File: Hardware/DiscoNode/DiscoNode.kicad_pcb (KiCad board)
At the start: 2 copper layers, 76 x 76 mm, 71 parts, among them IC1 ATMEGA328P, J1 1267, J2 RJ45, J3 RJ45, J4 AVR-ISP-6, J5 Debug, J6 0026605020, Q1 NTR4003N, Q2 NTR4003N, Q3 NTR4003N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

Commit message: Fix LEDs
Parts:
- D1, D10, D11, D12, D13, D14, D15, D16, D17, D18, D2, D3, D4, D5, D6, D7, D8, D9: footprint LEDs:LED_RGB_PLCC-6 -> LEDs:LED_WS2812-PLCC6
- moved R8 1.78 mm to (124.0, 58.1)
- moved R7 1.72 mm to (126.0, 58.1)
- moved R17 1.63 mm to (151.1, 118.0)
- moved R16 1.60 mm to (149.1, 118.0)
- moved R9 1.05 mm to (129.8, 52.8)
- moved R13 1.03 mm to (170.6, 110.4)
- moved R14 1.03 mm to (172.4, 110.4)
- moved R15 1.03 mm to (174.3, 110.4)
- moved R10 1.00 mm to (170.3, 65.4)
- moved R11 1.00 mm to (172.2, 65.4)
- moved R12 1.00 mm to (174.1, 65.4)
- moved R18 0.96 mm to (145.2, 123.5), turned to 270 degrees
- moved D16 0.78 mm to (172.4, 119.5)
- moved R1 0.75 mm to (105.9, 114.5)
- moved R2 0.75 mm to (103.9, 114.5)
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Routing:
- net Net-(D8-Pad3): track 11.9 -> 0.00 mm
- net Net-(D8-Pad2): track 11.9 -> 0.00 mm
- net Net-(D8-Pad1): track 11.9 -> 0.00 mm
- net /LEDR: track 279.5 -> 283.3 mm
- net /LEDG: track 222.9 -> 219.5 mm
- net +12V: track 354.1 -> 350.8 mm
- net Net-(D11-Pad1): track 7.33 -> 4.04 mm
- net Net-(D7-Pad1): track 6.33 -> 3.39 mm
- net /LEDB: track 202.8 -> 200.3 mm
- net Net-(D11-Pad2): track 9.20 -> 7.06 mm
- net Net-(D16-Pad1): track 5.49 -> 3.46 mm
- net Net-(D5-Pad3): track 11.9 -> 10.0 mm
- net Net-(D5-Pad2): track 11.9 -> 10.0 mm
- net Net-(D5-Pad1): track 11.9 -> 10.0 mm
- net Net-(D4-Pad3): track 11.9 -> 10.0 mm
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
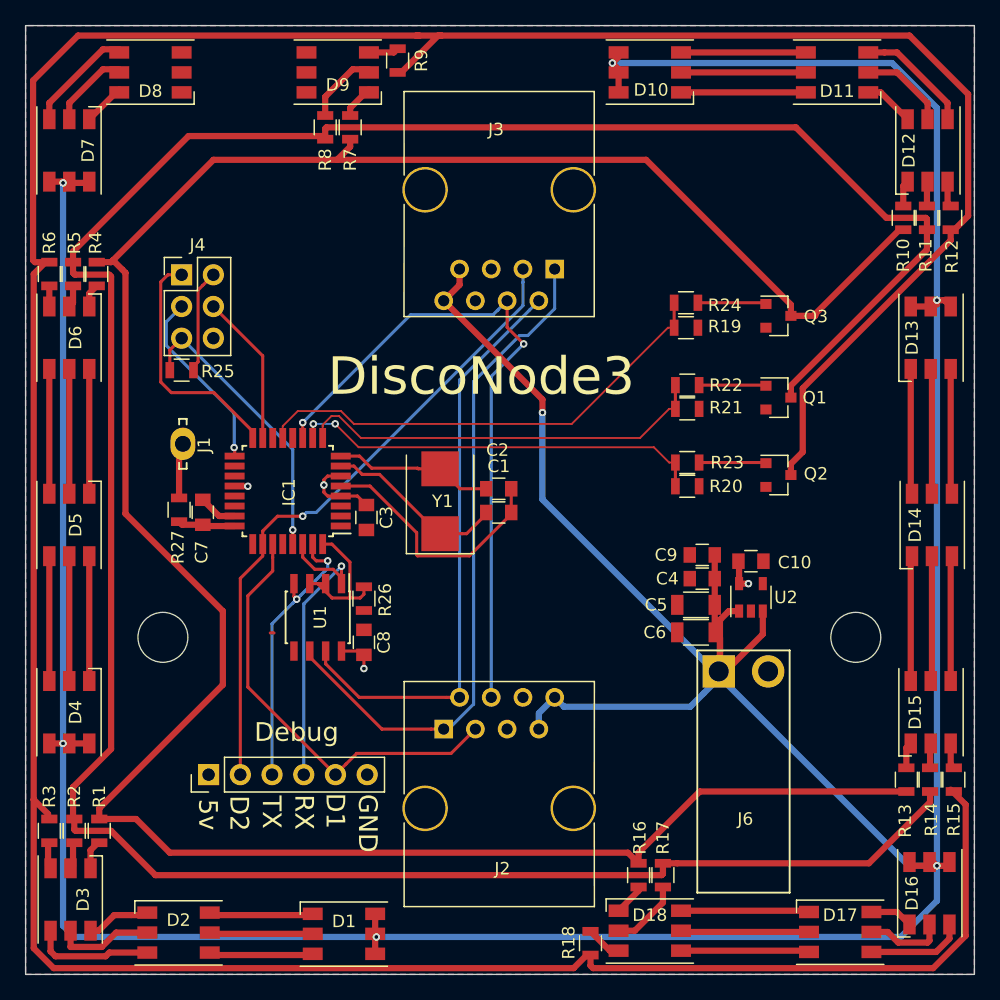
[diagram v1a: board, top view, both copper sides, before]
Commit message: Update LED & Crystal footprints. Change LED resistor placement.
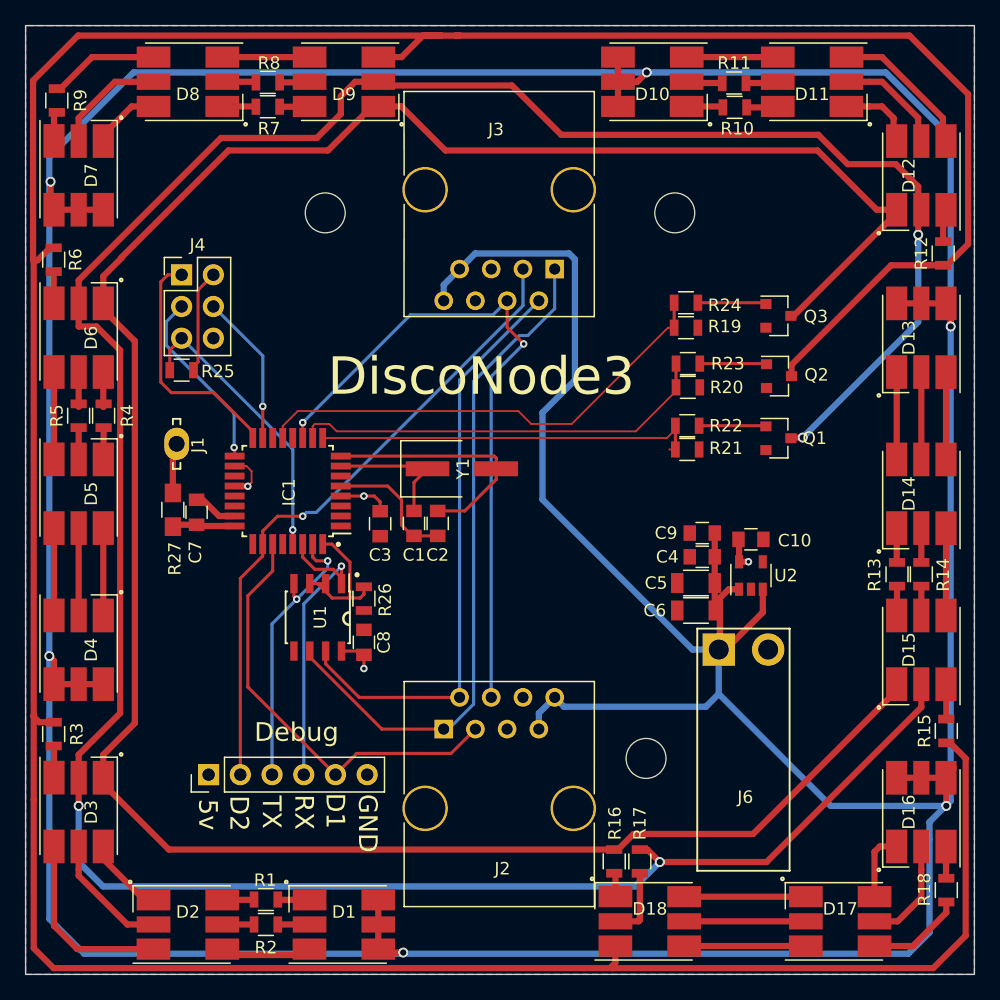
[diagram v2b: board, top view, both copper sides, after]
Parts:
- removed REF** (x2): MountingHole_4mm, Mounting_Holes:MountingHole_4mm
- added HOLE: MountingHole_3.2mm_M3, Mounting_Holes:MountingHole_3.2mm_M3, F.Cu at (152.0, 65.0)
- added HOLE: MountingHole_3.2mm_M3, Mounting_Holes:MountingHole_3.2mm_M3, F.Cu at (149.7, 108.7)
- added HOLE: MountingHole_3.2mm_M3, Mounting_Holes:MountingHole_3.2mm_M3, F.Cu at (124.0, 65.0)
- D1, D10, D11, D12, D13, D14, D15, D16, D17, D18, D2, D3, D4, D5, D6, D7, D8, D9: footprint LEDs:LED_WS2812-PLCC6 -> DiscoNode:LED_RGB-PLCC6-5.5x5.3mm
- IC1: value ATMEGA328P -> ATMEGA328PB-A
- R27: footprint Resistors_SMD:R_0805 -> Resistors_SMD:R_0805_HandSoldering
- Y1: footprint Crystals:Crystal_SMD_7050-2pin_7.0x5.0mm -> DiscoNode:Crystal_SMD_2pin_7.0x4.1mm
- moved R18 28.8 mm to (173.8, 119.2)
- moved R9 27.5 mm to (102.5, 56.0)
- moved R11 18.9 mm to (156.8, 54.6), turned to 0 degrees
- moved R2 17.1 mm to (119.2, 122.0), turned to 180 degrees
- moved R13 16.5 mm to (169.8, 94.0)
- moved R14 16.5 mm to (171.8, 94.0)
- moved R10 16.1 mm to (156.8, 56.5), turned to 0 degrees
- moved R1 14.4 mm to (119.2, 120.0), turned to 180 degrees
- moved R4 11.4 mm to (106.2, 81.2)
- moved R5 11.4 mm to (104.2, 81.2)
- moved R20 7.93 mm to (153.1, 79.0)
- moved Q2 7.93 mm to (160.3, 78.1)
- moved R23 7.93 mm to (153.1, 77.1)
- moved R3 7.76 mm to (102.2, 106.8)
- moved D3 7.03 mm to (104.2, 113.0)
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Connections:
- D11 pad 5: Net-(D10-Pad2) -> Net-(D11-Pad5)
- D11 pad 6: Net-(D10-Pad1) -> Net-(D11-Pad6)
- D12 pad 1: Net-(D12-Pad1) -> /LEDB
- D12 pad 2: Net-(D12-Pad2) -> /LEDG
- D15 pad 1: Net-(D15-Pad1) -> /LEDB
- D15 pad 2: Net-(D15-Pad2) -> /LEDG
- D15 pad 5: Net-(D14-Pad2) -> Net-(D15-Pad5)
- D15 pad 6: Net-(D14-Pad1) -> Net-(D15-Pad6)
- D17 pad 4: Net-(D16-Pad3) -> Net-(D17-Pad4)
- D18 pad 3: Net-(D18-Pad3) -> /LEDR
- D2 pad 5: Net-(D1-Pad2) -> Net-(D2-Pad5)
- D2 pad 6: Net-(D1-Pad1) -> Net-(D2-Pad6)
- D3 pad 1: Net-(D3-Pad1) -> /LEDB
- D3 pad 2: Net-(D3-Pad2) -> /LEDG
- D6 pad 1: Net-(D6-Pad1) -> /LEDB
- D6 pad 2: Net-(D6-Pad2) -> /LEDG
- D6 pad 5: Net-(D5-Pad2) -> Net-(D6-Pad5)
- D6 pad 6: Net-(D5-Pad1) -> Net-(D6-Pad6)
- D8 pad 4: Net-(D7-Pad3) -> Net-(D8-Pad4)
- D9 pad 1: Net-(D9-Pad1) -> /LEDB
- D9 pad 2: Net-(D9-Pad2) -> /LEDG
- D9 pad 3: Net-(D9-Pad3) -> /LEDR
- D9 pad 4: Net-(D8-Pad3) -> Net-(D9-Pad4)
- D9 pad 5: Net-(D8-Pad2) -> Net-(D9-Pad5)
- D9 pad 6: Net-(D8-Pad1) -> Net-(D9-Pad6)
- IC1 pad 3: GND -> Net-(IC1-Pad3)
- IC1 pad 6: +5V -> Net-(IC1-Pad6)
- R1 pad 1: Net-(D3-Pad1) -> Net-(D1-Pad1)
- R1 pad 2: /LEDB -> Net-(D2-Pad6)
- R10 pad 1: Net-(D12-Pad1) -> Net-(D10-Pad1)
- R10 pad 2: /LEDB -> Net-(D11-Pad6)
- R11 pad 1: Net-(D12-Pad2) -> Net-(D10-Pad2)
- R11 pad 2: /LEDG -> Net-(D11-Pad5)
- R13 pad 1: Net-(D15-Pad1) -> Net-(D14-Pad1)
- R13 pad 2: /LEDB -> Net-(D15-Pad6)
- R14 pad 1: Net-(D15-Pad2) -> Net-(D14-Pad2)
- R14 pad 2: /LEDG -> Net-(D15-Pad5)
- R18 pad 1: Net-(D18-Pad3) -> Net-(D16-Pad3)
- R18 pad 2: /LEDR -> Net-(D17-Pad4)
- R2 pad 1: Net-(D3-Pad2) -> Net-(D1-Pad2)
- R2 pad 2: /LEDG -> Net-(D2-Pad5)
- R4 pad 1: Net-(D6-Pad1) -> Net-(D5-Pad1)
- R4 pad 2: /LEDB -> Net-(D6-Pad6)
- R5 pad 1: Net-(D6-Pad2) -> Net-(D5-Pad2)
- R5 pad 2: /LEDG -> Net-(D6-Pad5)
- R7 pad 1: Net-(D9-Pad1) -> Net-(R7-Pad1)
- R7 pad 2: /LEDB -> Net-(D9-Pad6)
- R8 pad 1: Net-(D9-Pad2) -> Net-(R8-Pad1)
- R8 pad 2: /LEDG -> Net-(D9-Pad5)
- R9 pad 1: Net-(D9-Pad3) -> Net-(D8-Pad4)
- R9 pad 2: /LEDR -> Net-(D7-Pad3)
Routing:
- net +12V: track 350.8 -> 430.7 mm, vias 7 -> 6
- net /LEDG: track 219.5 -> 231.4 mm, vias 0 -> 4
- net GNDA: track 20.4 -> 10.6 mm
- net Net-(D8-Pad4): track 0.00 -> 8.80 mm
- net Net-(D17-Pad4): track 0.00 -> 7.71 mm
- net Net-(D5-Pad2): track 10.0 -> 2.30 mm
- net Net-(D5-Pad1): track 10.0 -> 2.31 mm
- net Net-(D14-Pad2): track 10.0 -> 2.75 mm
- net Net-(D14-Pad1): track 10.0 -> 2.76 mm
- net /X2: track 12.7 -> 20.0 mm
- net Net-(D10-Pad2): track 10.0 -> 2.89 mm
- net Net-(D10-Pad1): track 10.0 -> 2.93 mm
- net Net-(D8-Pad3): track 0.00 -> 6.99 mm
- net Net-(D7-Pad3): track 8.68 -> 2.38 mm
- net Net-(D16-Pad3): track 8.72 -> 2.55 mm
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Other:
- board text added: "Jeremy Gillick April 2017 http://bit.ly/2pooffX"
- board text removed: "Jeremy Gillick March 2017"

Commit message: Move RJ45 jacks to edge of board.
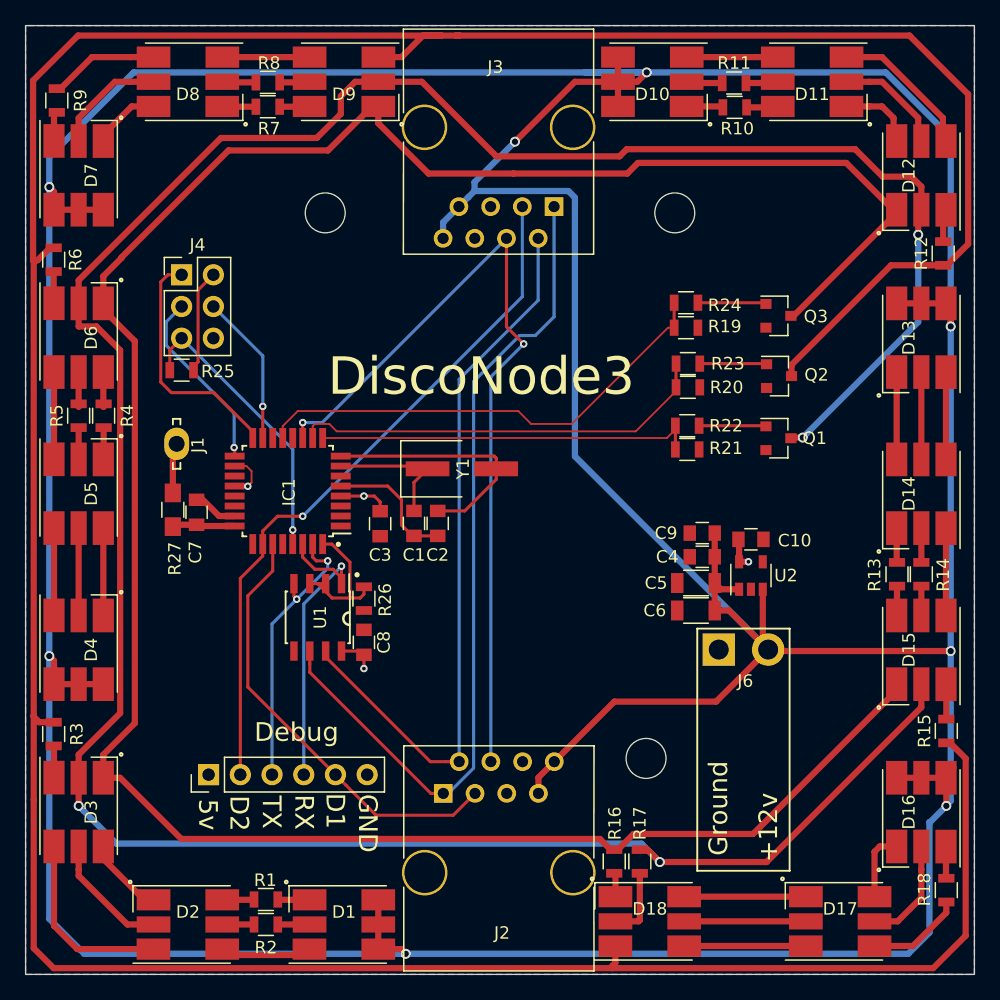
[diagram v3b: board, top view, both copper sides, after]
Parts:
- moved J2 5.15 mm to (133.5, 111.5)
- moved J3 5.00 mm to (142.3, 64.5)
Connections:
- D9 pad 4: Net-(D9-Pad4) -> Net-(D8-Pad3)
- J6 pad 1: +12V -> GND
- J6 pad 2: GND -> +12V
- R7 pad 1: Net-(R7-Pad1) -> Net-(D8-Pad1)
- R8 pad 1: Net-(R8-Pad1) -> Net-(D8-Pad2)
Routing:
- net +12V: track 430.7 -> 447.2 mm, vias 6 -> 8
- net /A/Y: track 54.7 -> 68.5 mm
- net /SharedSignal: track 55.0 -> 67.3 mm
- net /B/Z: track 47.3 -> 59.2 mm
- net /Daisy2: track 51.5 -> 56.0 mm
- net /LEDG: track 231.4 -> 228.4 mm
- net /LEDB: track 198.8 -> 200.5 mm
- net /Daisy1: track 34.9 -> 35.5 mm
- net /G: track 31.2 -> 30.7 mm
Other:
- board text added: "+12"
- board text added: "+12v"
- board text added: "-"
- board text added: "A/Y"
- board text added: "B/Z"
- board text added: "Ground"
- board text added: "S"

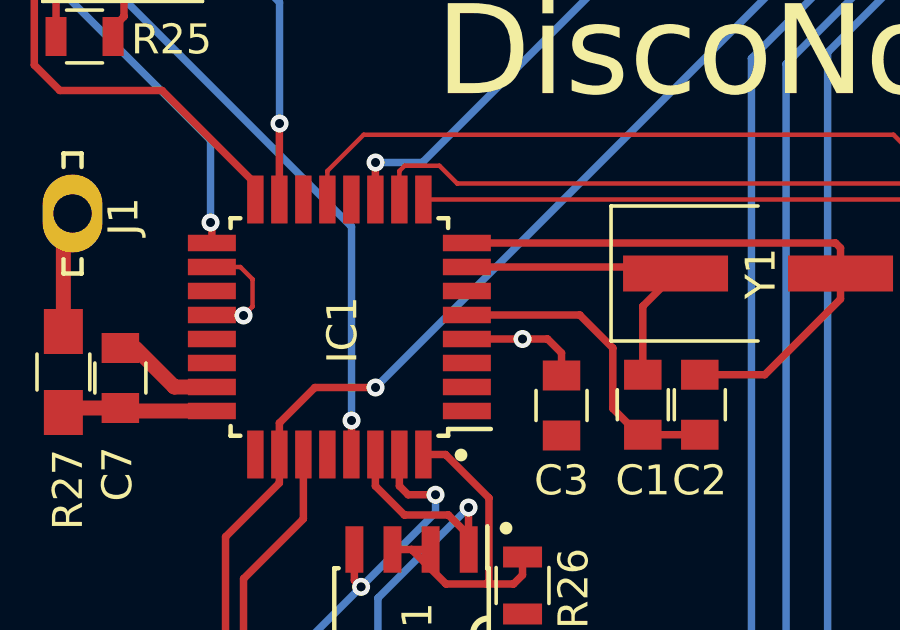
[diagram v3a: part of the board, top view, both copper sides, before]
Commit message: Move parts around. Better LED layout. Move RJ45 jacks to edge of board
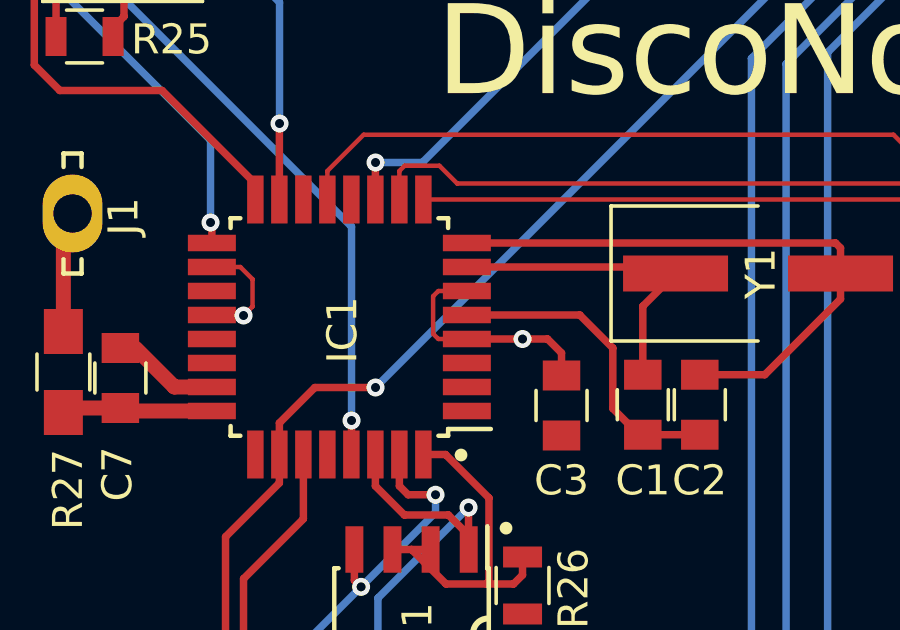
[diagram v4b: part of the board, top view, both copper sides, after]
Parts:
- IC1: value ATMEGA328PB-A -> ATMEGA328P-AU
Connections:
- IC1 pad 3: Net-(IC1-Pad3) -> GND
- IC1 pad 6: Net-(IC1-Pad6) -> +5V
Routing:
- net +5V: track 21.9 -> 25.6 mm
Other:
- board text added: "Jeremy Gillick May 2017 http://bit.ly/2pooffX"
- board text removed: "Jeremy Gillick April 2017 http://bit.ly/2pooffX"

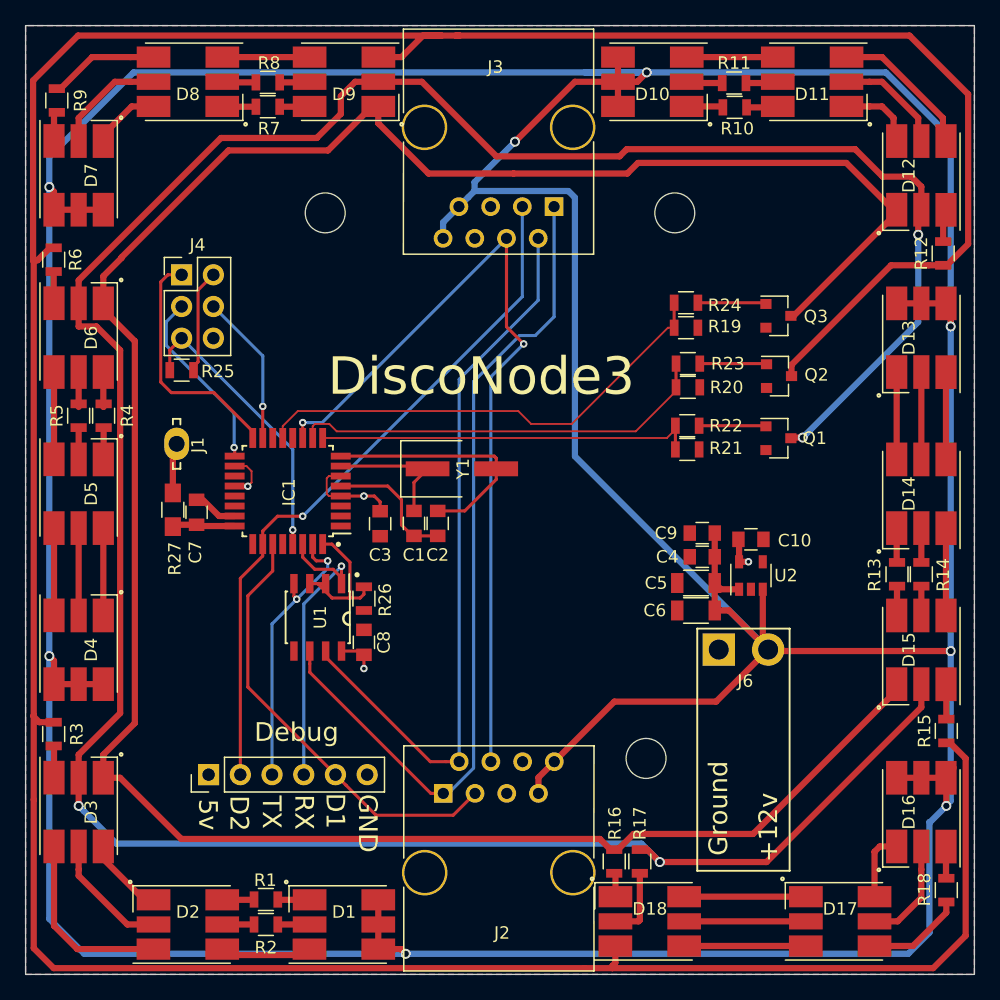
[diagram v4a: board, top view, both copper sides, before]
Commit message: Move debug pins.
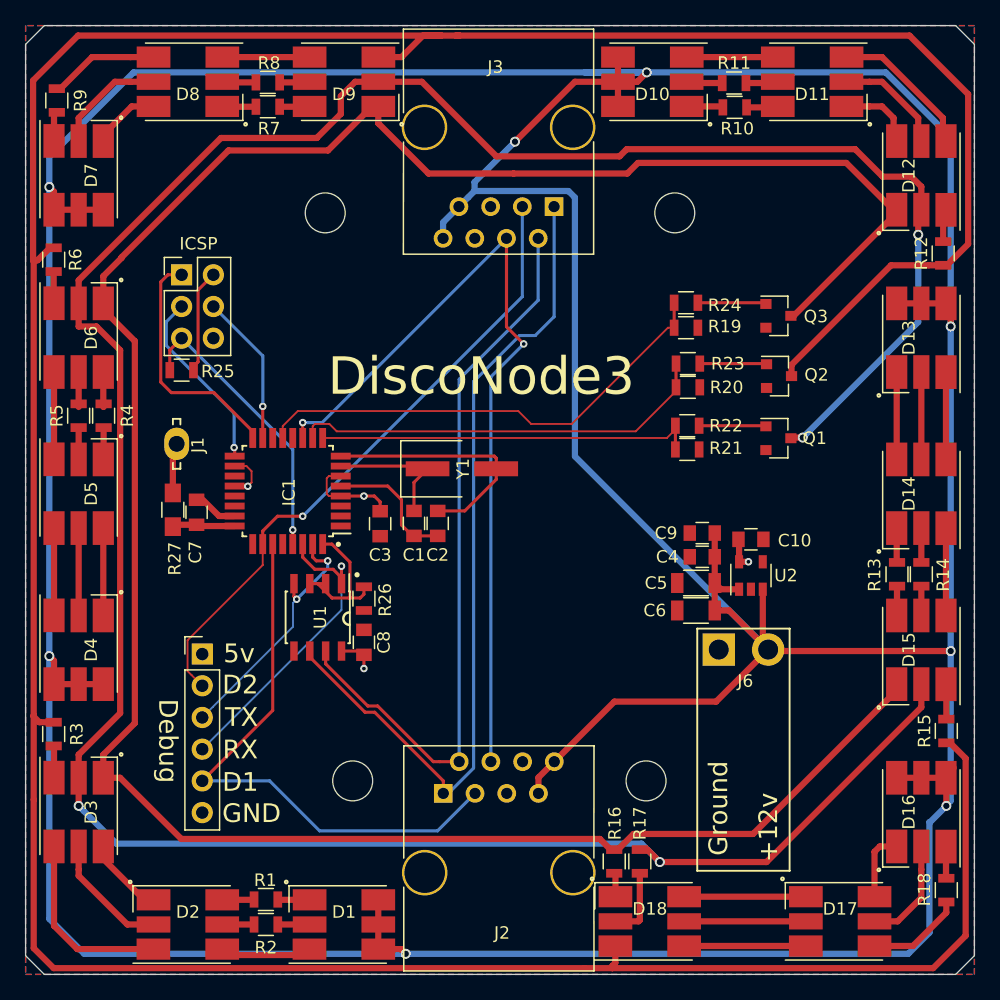
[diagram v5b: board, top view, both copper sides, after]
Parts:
- added HOLE: MountingHole_3.2mm_M3, Mounting_Holes:MountingHole_3.2mm_M3, F.Cu at (126.2, 110.5)
- R1, R10, R13, R16, R4, R7: value 330 -> 120
- R12, R15, R18, R3, R6, R9: value 120 -> 330
- moved J5 9.67 mm to (114.2, 100.3), turned to 0 degrees
- moved HOLE 1.80 mm to (149.7, 110.5)
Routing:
- net /Daisy1: track 35.5 -> 46.1 mm
- net /Daisy2: track 56.0 -> 51.2 mm
- net /TX: track 23.6 -> 21.4 mm
- net /RX: track 24.7 -> 26.0 mm
- net /B/Z: track 59.2 -> 60.0 mm
- net /A/Y: track 68.5 -> 67.9 mm
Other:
- outline, holes or cut-outs redrawn
- board text added: "ICSP"
- board text added: "Jeremy Gillick rev 3.2 (June 2016) http://bit.ly/2pooffX"
- board text removed: "Jeremy Gillick May 2017 http://bit.ly/2pooffX"
